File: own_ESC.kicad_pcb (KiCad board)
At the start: 2 copper layers, 61 x 99.6 mm, 144 parts, among them IC1 EFM8BB21F16G-C-QSOP24R, J1 SIGNAL PAD, J2 +BAT PAD, J3 -BAT PAD, J4 RX PAD, J5 CLK PAD, J6 A PAD, J7 B PAD, J8 C PAD, Q1 TPH1R403NL,L1Q, Q2 TPH1R403NL,L1Q, Q3 TPH1R403NL,L1Q, Q4 TPH1R403NL,L1Q, Q5 TPH1R403NL,L1Q, Q6 TPH1R403NL,L1Q, U1 FD6288T, U2 LM1117-5.0, U3 LM1117-3.3

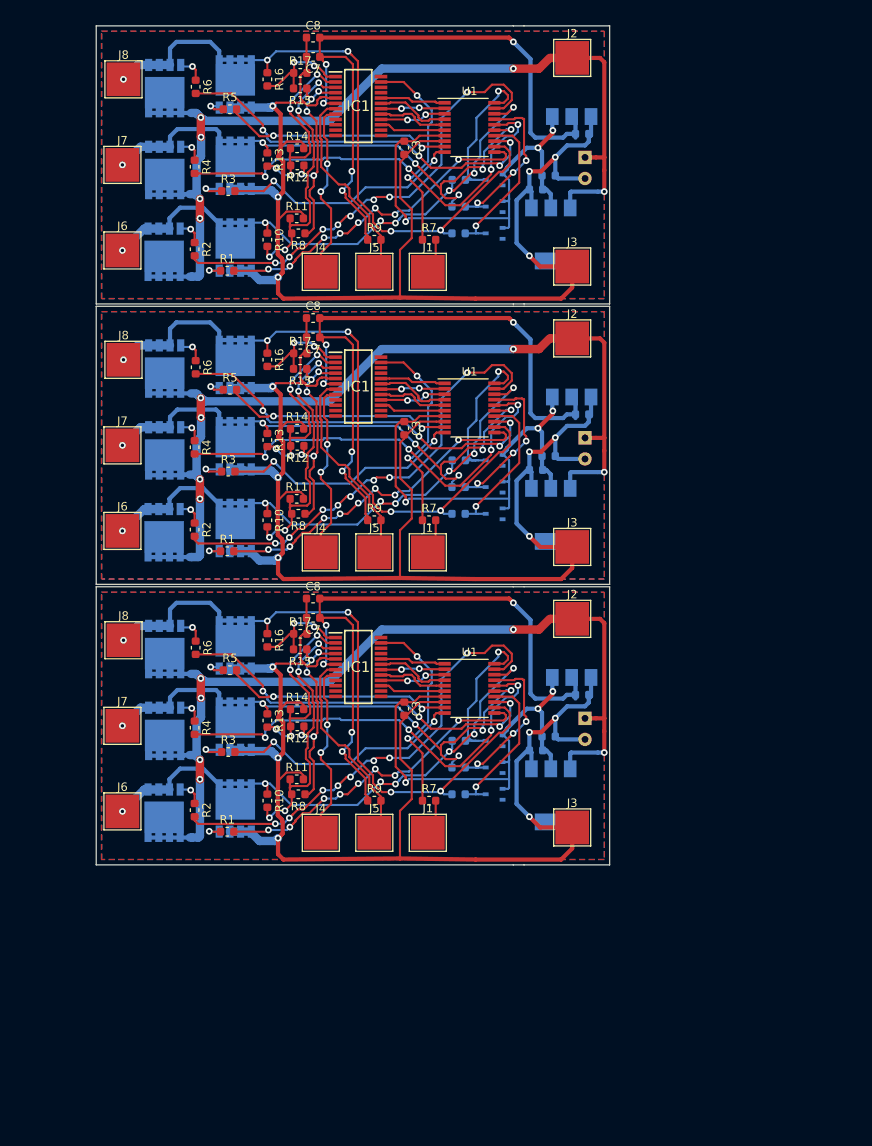
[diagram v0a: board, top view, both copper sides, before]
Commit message: Reduction of circuit area.
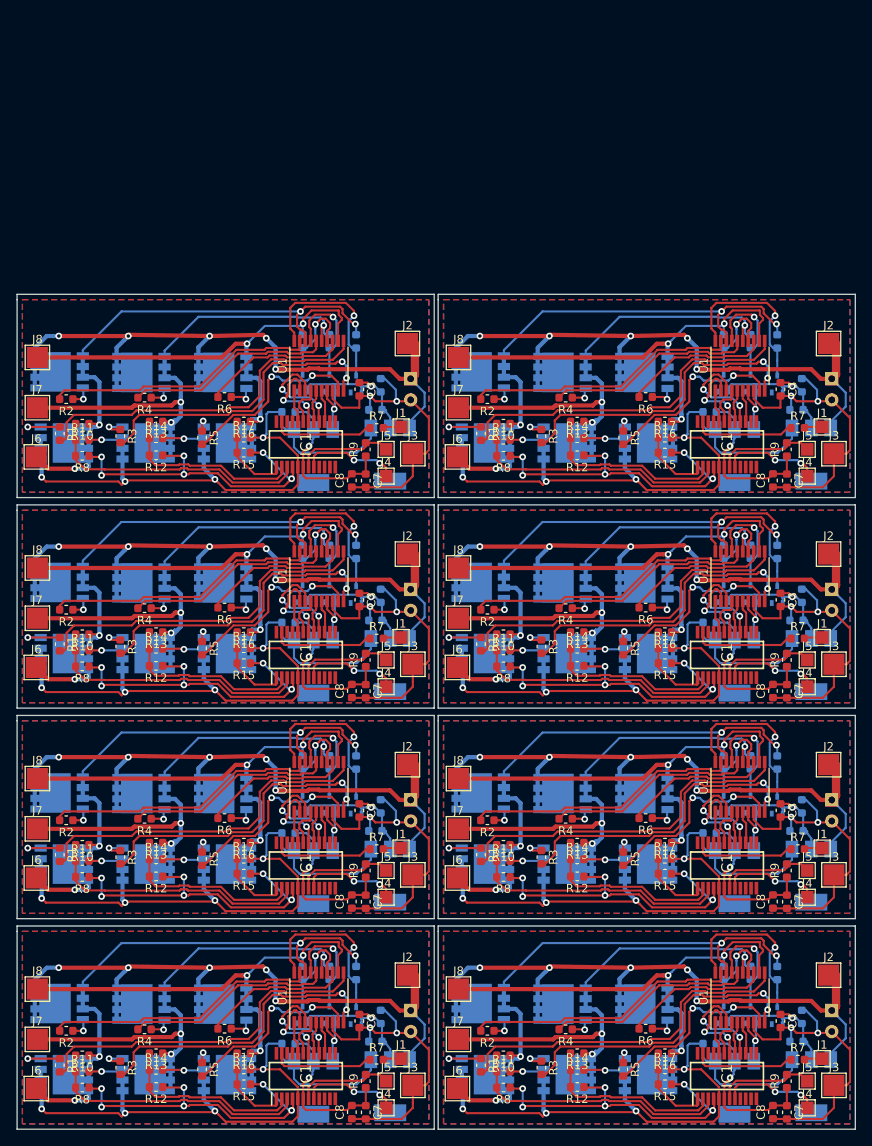
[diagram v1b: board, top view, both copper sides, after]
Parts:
- removed the C1 at (93.7, 118.4)
- removed the C1 at (93.7, 85.1)
- removed the C10 at (108.4, 113.0)
- removed the C10 at (108.4, 79.7)
- removed the C2 at (93.7, 121.6)
- removed the C2 at (93.7, 88.3)
- removed the C3 at (87.2, 114.6)
- removed the C3 at (87.2, 81.3)
- removed the C4 at (93.7, 124.8)
- removed the C4 at (93.7, 91.5)
- removed the C5 at (108.7, 115.7)
- removed the C5 at (108.7, 82.4)
- removed the C6 at (102.9, 119.6)
- removed the C6 at (102.9, 86.3)
- removed the C7 at (76.4, 103.8)
- removed the C7 at (76.4, 70.5)
- removed the C8 at (76.4, 101.5)
- removed the C8 at (76.4, 68.2)
- removed the C9 at (104.4, 117.9)
- removed the C9 at (104.4, 84.6)
- removed the D1 at (97.9, 118.4)
- removed the D1 at (97.9, 85.1)
- removed the D2 at (97.9, 121.6)
- removed the D2 at (97.9, 88.3)
- removed the D3 at (97.9, 124.8)
- removed the D3 at (97.9, 91.5)
- removed the IC1 at (81.8, 109.7)
- removed the IC1 at (81.8, 76.4)
- removed the J1 at (90.0, 129.3)
- removed the J1 at (90.0, 96.0)
- removed the J1 at (90.0, 62.7)
- removed the J2 at (107.2, 103.9)
- removed the J2 at (107.2, 70.6)
- removed the J2 at (107.2, 37.3)
- removed the J3 at (107.2, 128.7)
- removed the J3 at (107.2, 95.4)
- removed the J3 at (107.2, 62.1)
- removed the J4 at (77.3, 129.3)
- removed the J4 at (77.3, 96.0)
- removed the J4 at (77.3, 62.7)
- removed the J5 at (83.7, 129.3)
- removed the J5 at (83.7, 96.0)
- removed the J5 at (83.7, 62.7)
- removed the J6 at (53.8, 126.8)
- removed the J6 at (53.8, 93.5)
- removed the J6 at (53.8, 60.2)
- removed the J7 at (53.8, 116.6)
- removed the J7 at (53.8, 83.3)
- removed the J7 at (53.8, 50.0)
- removed the J8 at (53.9, 106.5)
- removed the J8 at (53.9, 73.2)
- removed the J8 at (53.9, 39.9)
- removed the Q1 at (67.2, 126.3)
- removed the Q1 at (67.2, 93.0)
- removed the Q2 at (58.7, 127.1)
- removed the Q2 at (58.7, 93.8)
- removed the Q3 at (67.2, 116.6)
- removed the Q3 at (67.2, 83.3)
- removed the Q4 at (58.8, 117.3)
- removed the Q4 at (58.8, 84.0)
- removed the Q5 at (67.2, 107.0)
- removed the Q5 at (67.2, 73.7)
- removed the Q6 at (58.8, 107.6)
- removed the Q6 at (58.8, 74.3)
- removed the R1 at (66.2, 129.2)
- removed the R1 at (66.2, 95.9)
- removed the R10 at (71.0, 125.5)
- removed the R10 at (71.0, 92.2)
- removed the R11 at (74.5, 123.0)
- removed the R11 at (74.5, 89.7)
- removed the R12 at (74.5, 116.7)
- removed the R12 at (74.5, 83.4)
- removed the R13 at (71.0, 116.0)
- removed the R13 at (71.0, 82.7)
- removed the R14 at (74.5, 114.7)
- removed the R14 at (74.5, 81.4)
- removed the R15 at (74.9, 107.6)
- removed the R15 at (74.9, 74.3)
- removed the R16 at (71.0, 106.5)
- removed the R16 at (71.0, 73.2)
- removed the R17 at (74.9, 105.7)
- removed the R17 at (74.9, 72.4)
- removed the R2 at (62.4, 126.6)
- removed the R2 at (62.4, 93.3)
- removed the R3 at (66.4, 119.7)
- removed the R3 at (66.4, 86.4)
- removed the R4 at (62.4, 116.9)
- removed the R4 at (62.4, 83.6)
- removed the R5 at (66.5, 110.0)
- removed the R5 at (66.5, 76.7)
- removed the R6 at (62.5, 107.4)
- removed the R6 at (62.5, 74.1)
- removed the R7 at (90.2, 125.5)
- removed the R7 at (90.2, 92.2)
- removed the R8 at (74.7, 124.8)
- removed the R8 at (74.7, 91.5)
- removed the R9 at (83.7, 125.5)
- removed the R9 at (83.7, 92.2)
- removed the U1 at (95.0, 112.2)
- removed the U1 at (95.0, 78.9)
- removed the U2 at (104.6, 124.9)
- removed the U2 at (104.6, 91.6)
- removed the U3 at (107.1, 107.7)
- removed the U3 at (107.1, 74.4)
- added C1: 1uF, Capacitor_SMD:C_0603_1608Metric, B.Cu at (131.5, 146.0)
- added C1: 1uF, Capacitor_SMD:C_0603_1608Metric, B.Cu at (81.5, 146.0)
- added C1: 1uF, Capacitor_SMD:C_0603_1608Metric, B.Cu at (131.5, 121.0)
- added C1: 1uF, Capacitor_SMD:C_0603_1608Metric, B.Cu at (81.5, 121.0)
- added C1: 1uF, Capacitor_SMD:C_0603_1608Metric, B.Cu at (131.5, 96.0)
- added C1: 1uF, Capacitor_SMD:C_0603_1608Metric, B.Cu at (81.5, 96.0)
- added C1: 1uF, Capacitor_SMD:C_0603_1608Metric, B.Cu at (131.5, 71.0)
- added C10: 10uF, Capacitor_SMD:C_0603_1608Metric, B.Cu at (123.5, 154.4)
- added C10: 10uF, Capacitor_SMD:C_0603_1608Metric, B.Cu at (73.5, 154.4)
- added C10: 10uF, Capacitor_SMD:C_0603_1608Metric, B.Cu at (123.5, 129.4)
- added C10: 10uF, Capacitor_SMD:C_0603_1608Metric, B.Cu at (73.5, 129.4)
- added C10: 10uF, Capacitor_SMD:C_0603_1608Metric, B.Cu at (123.5, 104.4)
- added C10: 10uF, Capacitor_SMD:C_0603_1608Metric, B.Cu at (73.5, 104.4)
- added C10: 10uF, Capacitor_SMD:C_0603_1608Metric, B.Cu at (123.5, 79.4)
- added C2: 1uF, Capacitor_SMD:C_0603_1608Metric, B.Cu at (128.4, 146.0)
- added C2: 1uF, Capacitor_SMD:C_0603_1608Metric, B.Cu at (78.4, 146.0)
- added C2: 1uF, Capacitor_SMD:C_0603_1608Metric, B.Cu at (128.4, 121.0)
- added C2: 1uF, Capacitor_SMD:C_0603_1608Metric, B.Cu at (78.4, 121.0)
- added C2: 1uF, Capacitor_SMD:C_0603_1608Metric, B.Cu at (128.4, 96.0)
- added C2: 1uF, Capacitor_SMD:C_0603_1608Metric, B.Cu at (78.4, 96.0)
- added C2: 1uF, Capacitor_SMD:C_0603_1608Metric, B.Cu at (128.4, 71.0)
- added C3: 10uF, Capacitor_SMD:C_0603_1608Metric, F.Cu at (131.9, 151.7)
- added C3: 10uF, Capacitor_SMD:C_0603_1608Metric, F.Cu at (81.9, 151.7)
- added C3: 10uF, Capacitor_SMD:C_0603_1608Metric, F.Cu at (131.9, 126.7)
- added C3: 10uF, Capacitor_SMD:C_0603_1608Metric, F.Cu at (81.9, 126.7)
- added C3: 10uF, Capacitor_SMD:C_0603_1608Metric, F.Cu at (131.9, 101.7)
- added C3: 10uF, Capacitor_SMD:C_0603_1608Metric, F.Cu at (81.9, 101.7)
- added C3: 10uF, Capacitor_SMD:C_0603_1608Metric, F.Cu at (131.9, 76.7)
- added C4: 1uF, Capacitor_SMD:C_0603_1608Metric, B.Cu at (125.2, 146.0)
- added C4: 1uF, Capacitor_SMD:C_0603_1608Metric, B.Cu at (75.2, 146.0)
- added C4: 1uF, Capacitor_SMD:C_0603_1608Metric, B.Cu at (125.2, 121.0)
- added C4: 1uF, Capacitor_SMD:C_0603_1608Metric, B.Cu at (75.2, 121.0)
- added C4: 1uF, Capacitor_SMD:C_0603_1608Metric, B.Cu at (125.2, 96.0)
- added C4: 1uF, Capacitor_SMD:C_0603_1608Metric, B.Cu at (75.2, 96.0)
- added C4: 1uF, Capacitor_SMD:C_0603_1608Metric, B.Cu at (125.2, 71.0)
- added C5: 10uF, Capacitor_THT:CP_Radial_D5.0mm_P2.50mm, B.Cu at (138.0, 150.4)
- added C5: 10uF, Capacitor_THT:CP_Radial_D5.0mm_P2.50mm, B.Cu at (88.0, 150.4)
- added C5: 10uF, Capacitor_THT:CP_Radial_D5.0mm_P2.50mm, B.Cu at (138.0, 125.4)
- added C5: 10uF, Capacitor_THT:CP_Radial_D5.0mm_P2.50mm, B.Cu at (88.0, 125.4)
- added C5: 10uF, Capacitor_THT:CP_Radial_D5.0mm_P2.50mm, B.Cu at (138.0, 100.4)
- added C5: 10uF, Capacitor_THT:CP_Radial_D5.0mm_P2.50mm, B.Cu at (88.0, 100.4)
- added C5: 10uF, Capacitor_THT:CP_Radial_D5.0mm_P2.50mm, B.Cu at (138.0, 75.4)
- added C6: 10uF, Capacitor_SMD:C_0603_1608Metric, B.Cu at (133.8, 154.1)
- added C6: 10uF, Capacitor_SMD:C_0603_1608Metric, B.Cu at (83.8, 154.1)
- added C6: 10uF, Capacitor_SMD:C_0603_1608Metric, B.Cu at (133.8, 129.1)
- added C6: 10uF, Capacitor_SMD:C_0603_1608Metric, B.Cu at (83.8, 129.1)
- added C6: 10uF, Capacitor_SMD:C_0603_1608Metric, B.Cu at (133.8, 104.1)
- added C6: 10uF, Capacitor_SMD:C_0603_1608Metric, B.Cu at (83.8, 104.1)
- added C6: 10uF, Capacitor_SMD:C_0603_1608Metric, B.Cu at (133.8, 79.1)
- added C7: 0.1uF, Capacitor_SMD:C_0603_1608Metric, F.Cu at (132.7, 162.5)
- added C7: 0.1uF, Capacitor_SMD:C_0603_1608Metric, F.Cu at (82.7, 162.5)
- added C7: 0.1uF, Capacitor_SMD:C_0603_1608Metric, F.Cu at (132.7, 137.5)
- added C7: 0.1uF, Capacitor_SMD:C_0603_1608Metric, F.Cu at (82.7, 137.5)
- added C7: 0.1uF, Capacitor_SMD:C_0603_1608Metric, F.Cu at (132.7, 112.5)
- added C7: 0.1uF, Capacitor_SMD:C_0603_1608Metric, F.Cu at (82.7, 112.5)
- added C7: 0.1uF, Capacitor_SMD:C_0603_1608Metric, F.Cu at (132.7, 87.5)
- added C8: 4.7uF, Capacitor_SMD:C_0603_1608Metric, F.Cu at (131.0, 162.5)
- added C8: 4.7uF, Capacitor_SMD:C_0603_1608Metric, F.Cu at (81.0, 162.5)
- added C8: 4.7uF, Capacitor_SMD:C_0603_1608Metric, F.Cu at (131.0, 137.5)
- added C8: 4.7uF, Capacitor_SMD:C_0603_1608Metric, F.Cu at (81.0, 137.5)
- added C8: 4.7uF, Capacitor_SMD:C_0603_1608Metric, F.Cu at (131.0, 112.5)
- added C8: 4.7uF, Capacitor_SMD:C_0603_1608Metric, F.Cu at (81.0, 112.5)
- added C8: 4.7uF, Capacitor_SMD:C_0603_1608Metric, F.Cu at (131.0, 87.5)
- added C9: 10uF, Capacitor_SMD:C_0603_1608Metric, B.Cu at (134.5, 151.2)
- added C9: 10uF, Capacitor_SMD:C_0603_1608Metric, B.Cu at (84.5, 151.2)
- added C9: 10uF, Capacitor_SMD:C_0603_1608Metric, B.Cu at (134.5, 126.2)
- added C9: 10uF, Capacitor_SMD:C_0603_1608Metric, B.Cu at (84.5, 126.2)
- added C9: 10uF, Capacitor_SMD:C_0603_1608Metric, B.Cu at (134.5, 101.2)
- added C9: 10uF, Capacitor_SMD:C_0603_1608Metric, B.Cu at (84.5, 101.2)
- added C9: 10uF, Capacitor_SMD:C_0603_1608Metric, B.Cu at (134.5, 76.2)
- added D1: BAT54W, Package_TO_SOT_SMD:SOT-323_SC-70, B.Cu at (131.5, 151.1)
- added D1: BAT54W, Package_TO_SOT_SMD:SOT-323_SC-70, B.Cu at (81.5, 151.1)
- added D1: BAT54W, Package_TO_SOT_SMD:SOT-323_SC-70, B.Cu at (131.5, 126.1)
- added D1: BAT54W, Package_TO_SOT_SMD:SOT-323_SC-70, B.Cu at (81.5, 126.1)
- added D1: BAT54W, Package_TO_SOT_SMD:SOT-323_SC-70, B.Cu at (131.5, 101.1)
- added D1: BAT54W, Package_TO_SOT_SMD:SOT-323_SC-70, B.Cu at (81.5, 101.1)
- added D1: BAT54W, Package_TO_SOT_SMD:SOT-323_SC-70, B.Cu at (131.5, 76.1)
- added D2: BAT54W, Package_TO_SOT_SMD:SOT-323_SC-70, B.Cu at (128.4, 151.0)
- added D2: BAT54W, Package_TO_SOT_SMD:SOT-323_SC-70, B.Cu at (78.4, 151.0)
- added D2: BAT54W, Package_TO_SOT_SMD:SOT-323_SC-70, B.Cu at (128.4, 126.0)
- added D2: BAT54W, Package_TO_SOT_SMD:SOT-323_SC-70, B.Cu at (78.4, 126.0)
- added D2: BAT54W, Package_TO_SOT_SMD:SOT-323_SC-70, B.Cu at (128.4, 101.0)
- added D2: BAT54W, Package_TO_SOT_SMD:SOT-323_SC-70, B.Cu at (78.4, 101.0)
- added D2: BAT54W, Package_TO_SOT_SMD:SOT-323_SC-70, B.Cu at (128.4, 76.0)
- added D3: BAT54W, Package_TO_SOT_SMD:SOT-323_SC-70, B.Cu at (125.2, 151.0)
- added D3: BAT54W, Package_TO_SOT_SMD:SOT-323_SC-70, B.Cu at (75.2, 151.0)
- added D3: BAT54W, Package_TO_SOT_SMD:SOT-323_SC-70, B.Cu at (125.2, 126.0)
- added D3: BAT54W, Package_TO_SOT_SMD:SOT-323_SC-70, B.Cu at (75.2, 126.0)
- added D3: BAT54W, Package_TO_SOT_SMD:SOT-323_SC-70, B.Cu at (125.2, 101.0)
- added D3: BAT54W, Package_TO_SOT_SMD:SOT-323_SC-70, B.Cu at (75.2, 101.0)
- added D3: BAT54W, Package_TO_SOT_SMD:SOT-323_SC-70, B.Cu at (125.2, 76.0)
- added IC1: EFM8BB21F16G-C-QSOP24R, SOP64P600X175-24N, F.Cu at (125.6, 158.2)
- added IC1: EFM8BB21F16G-C-QSOP24R, SOP64P600X175-24N, F.Cu at (75.6, 158.2)
- added IC1: EFM8BB21F16G-C-QSOP24R, SOP64P600X175-24N, F.Cu at (125.6, 133.2)
- added IC1: EFM8BB21F16G-C-QSOP24R, SOP64P600X175-24N, F.Cu at (75.6, 133.2)
- added IC1: EFM8BB21F16G-C-QSOP24R, SOP64P600X175-24N, F.Cu at (125.6, 108.2)
- added IC1: EFM8BB21F16G-C-QSOP24R, SOP64P600X175-24N, F.Cu at (75.6, 108.2)
- added IC1: EFM8BB21F16G-C-QSOP24R, SOP64P600X175-24N, F.Cu at (125.6, 83.2)
- added J1: SIGNAL PAD, TestPoint:TestPoint_Pad_1.5x1.5mm, F.Cu at (136.9, 156.2)
- added J1: SIGNAL PAD, TestPoint:TestPoint_Pad_1.5x1.5mm, F.Cu at (86.9, 156.2)
- added J1: SIGNAL PAD, TestPoint:TestPoint_Pad_1.5x1.5mm, F.Cu at (136.9, 131.2)
- added J1: SIGNAL PAD, TestPoint:TestPoint_Pad_1.5x1.5mm, F.Cu at (86.9, 131.2)
- added J1: SIGNAL PAD, TestPoint:TestPoint_Pad_1.5x1.5mm, F.Cu at (136.9, 106.2)
- added J1: SIGNAL PAD, TestPoint:TestPoint_Pad_1.5x1.5mm, F.Cu at (86.9, 106.2)
- added J1: SIGNAL PAD, TestPoint:TestPoint_Pad_1.5x1.5mm, F.Cu at (136.9, 81.2)
- added J1: SIGNAL PAD, TestPoint:TestPoint_Pad_1.5x1.5mm, F.Cu at (86.9, 81.2)
- added J2: +BAT PAD, TestPoint:TestPoint_Pad_2.5x2.5mm, F.Cu at (137.6, 146.2)
- added J2: +BAT PAD, TestPoint:TestPoint_Pad_2.5x2.5mm, F.Cu at (87.6, 146.2)
- added J2: +BAT PAD, TestPoint:TestPoint_Pad_2.5x2.5mm, F.Cu at (137.6, 121.2)
- added J2: +BAT PAD, TestPoint:TestPoint_Pad_2.5x2.5mm, F.Cu at (87.6, 121.2)
- added J2: +BAT PAD, TestPoint:TestPoint_Pad_2.5x2.5mm, F.Cu at (137.6, 96.2)
- added J2: +BAT PAD, TestPoint:TestPoint_Pad_2.5x2.5mm, F.Cu at (87.6, 96.2)
- added J2: +BAT PAD, TestPoint:TestPoint_Pad_2.5x2.5mm, F.Cu at (137.6, 71.2)
- added J2: +BAT PAD, TestPoint:TestPoint_Pad_2.5x2.5mm, F.Cu at (87.6, 71.2)
- added J3: -BAT PAD, TestPoint:TestPoint_Pad_2.5x2.5mm, F.Cu at (138.3, 159.3)
- added J3: -BAT PAD, TestPoint:TestPoint_Pad_2.5x2.5mm, F.Cu at (88.3, 159.3)
- added J3: -BAT PAD, TestPoint:TestPoint_Pad_2.5x2.5mm, F.Cu at (138.3, 134.3)
- added J3: -BAT PAD, TestPoint:TestPoint_Pad_2.5x2.5mm, F.Cu at (88.3, 134.3)
- added J3: -BAT PAD, TestPoint:TestPoint_Pad_2.5x2.5mm, F.Cu at (138.3, 109.3)
- added J3: -BAT PAD, TestPoint:TestPoint_Pad_2.5x2.5mm, F.Cu at (88.3, 109.3)
- added J3: -BAT PAD, TestPoint:TestPoint_Pad_2.5x2.5mm, F.Cu at (138.3, 84.3)
- added J3: -BAT PAD, TestPoint:TestPoint_Pad_2.5x2.5mm, F.Cu at (88.3, 84.3)
- added J4: RX PAD, TestPoint:TestPoint_Pad_1.5x1.5mm, F.Cu at (135.1, 162.0)
- added J4: RX PAD, TestPoint:TestPoint_Pad_1.5x1.5mm, F.Cu at (85.1, 162.0)
- added J4: RX PAD, TestPoint:TestPoint_Pad_1.5x1.5mm, F.Cu at (135.1, 137.0)
- added J4: RX PAD, TestPoint:TestPoint_Pad_1.5x1.5mm, F.Cu at (85.1, 137.0)
- added J4: RX PAD, TestPoint:TestPoint_Pad_1.5x1.5mm, F.Cu at (135.1, 112.0)
- added J4: RX PAD, TestPoint:TestPoint_Pad_1.5x1.5mm, F.Cu at (85.1, 112.0)
- added J4: RX PAD, TestPoint:TestPoint_Pad_1.5x1.5mm, F.Cu at (135.1, 87.0)
- added J4: RX PAD, TestPoint:TestPoint_Pad_1.5x1.5mm, F.Cu at (85.1, 87.0)
- added J5: CLK PAD, TestPoint:TestPoint_Pad_1.5x1.5mm, F.Cu at (135.1, 158.8)
- added J5: CLK PAD, TestPoint:TestPoint_Pad_1.5x1.5mm, F.Cu at (85.1, 158.8)
- added J5: CLK PAD, TestPoint:TestPoint_Pad_1.5x1.5mm, F.Cu at (135.1, 133.8)
- added J5: CLK PAD, TestPoint:TestPoint_Pad_1.5x1.5mm, F.Cu at (85.1, 133.8)
- added J5: CLK PAD, TestPoint:TestPoint_Pad_1.5x1.5mm, F.Cu at (135.1, 108.8)
- added J5: CLK PAD, TestPoint:TestPoint_Pad_1.5x1.5mm, F.Cu at (85.1, 108.8)
- added J5: CLK PAD, TestPoint:TestPoint_Pad_1.5x1.5mm, F.Cu at (135.1, 83.8)
- added J5: CLK PAD, TestPoint:TestPoint_Pad_1.5x1.5mm, F.Cu at (85.1, 83.8)
- added J6: A PAD, TestPoint:TestPoint_Pad_2.5x2.5mm, F.Cu at (93.6, 159.7)
- added J6: A PAD, TestPoint:TestPoint_Pad_2.5x2.5mm, F.Cu at (43.6, 159.7)
- added J6: A PAD, TestPoint:TestPoint_Pad_2.5x2.5mm, F.Cu at (93.6, 134.7)
- added J6: A PAD, TestPoint:TestPoint_Pad_2.5x2.5mm, F.Cu at (43.6, 134.7)
- added J6: A PAD, TestPoint:TestPoint_Pad_2.5x2.5mm, F.Cu at (93.6, 109.7)
- added J6: A PAD, TestPoint:TestPoint_Pad_2.5x2.5mm, F.Cu at (43.6, 109.7)
- added J6: A PAD, TestPoint:TestPoint_Pad_2.5x2.5mm, F.Cu at (93.6, 84.7)
- added J6: A PAD, TestPoint:TestPoint_Pad_2.5x2.5mm, F.Cu at (43.6, 84.7)
- added J7: B PAD, TestPoint:TestPoint_Pad_2.5x2.5mm, F.Cu at (93.7, 153.9)
- added J7: B PAD, TestPoint:TestPoint_Pad_2.5x2.5mm, F.Cu at (43.7, 153.9)
- added J7: B PAD, TestPoint:TestPoint_Pad_2.5x2.5mm, F.Cu at (93.7, 128.9)
- added J7: B PAD, TestPoint:TestPoint_Pad_2.5x2.5mm, F.Cu at (43.7, 128.9)
- added J7: B PAD, TestPoint:TestPoint_Pad_2.5x2.5mm, F.Cu at (93.7, 103.9)
- added J7: B PAD, TestPoint:TestPoint_Pad_2.5x2.5mm, F.Cu at (43.7, 103.9)
- added J7: B PAD, TestPoint:TestPoint_Pad_2.5x2.5mm, F.Cu at (93.7, 78.9)
- added J7: B PAD, TestPoint:TestPoint_Pad_2.5x2.5mm, F.Cu at (43.7, 78.9)
- added J8: C PAD, TestPoint:TestPoint_Pad_2.5x2.5mm, F.Cu at (93.7, 147.9)
- added J8: C PAD, TestPoint:TestPoint_Pad_2.5x2.5mm, F.Cu at (43.7, 147.9)
- added J8: C PAD, TestPoint:TestPoint_Pad_2.5x2.5mm, F.Cu at (93.7, 122.9)
- added J8: C PAD, TestPoint:TestPoint_Pad_2.5x2.5mm, F.Cu at (43.7, 122.9)
- added J8: C PAD, TestPoint:TestPoint_Pad_2.5x2.5mm, F.Cu at (93.7, 97.9)
- added J8: C PAD, TestPoint:TestPoint_Pad_2.5x2.5mm, F.Cu at (43.7, 97.9)
- added J8: C PAD, TestPoint:TestPoint_Pad_2.5x2.5mm, F.Cu at (93.7, 72.9)
- added J8: C PAD, TestPoint:TestPoint_Pad_2.5x2.5mm, F.Cu at (43.7, 72.9)
- added Q1: TPH1R403NL,L1Q, TPH1R403NLL1Q, B.Cu at (96.9, 158.1)
- added Q1: TPH1R403NL,L1Q, TPH1R403NLL1Q, B.Cu at (46.9, 158.1)
- added Q1: TPH1R403NL,L1Q, TPH1R403NLL1Q, B.Cu at (96.9, 133.1)
- added Q1: TPH1R403NL,L1Q, TPH1R403NLL1Q, B.Cu at (46.9, 133.1)
- added Q1: TPH1R403NL,L1Q, TPH1R403NLL1Q, B.Cu at (96.9, 108.1)
- added Q1: TPH1R403NL,L1Q, TPH1R403NLL1Q, B.Cu at (46.9, 108.1)
- added Q1: TPH1R403NL,L1Q, TPH1R403NLL1Q, B.Cu at (96.9, 83.1)
- added Q2: TPH1R403NL,L1Q, TPH1R403NLL1Q, B.Cu at (96.2, 149.6)
- added Q2: TPH1R403NL,L1Q, TPH1R403NLL1Q, B.Cu at (46.2, 149.6)
- added Q2: TPH1R403NL,L1Q, TPH1R403NLL1Q, B.Cu at (96.2, 124.6)
- added Q2: TPH1R403NL,L1Q, TPH1R403NLL1Q, B.Cu at (46.2, 124.6)
- added Q2: TPH1R403NL,L1Q, TPH1R403NLL1Q, B.Cu at (96.2, 99.6)
- added Q2: TPH1R403NL,L1Q, TPH1R403NLL1Q, B.Cu at (46.2, 99.6)
- added Q2: TPH1R403NL,L1Q, TPH1R403NLL1Q, B.Cu at (96.2, 74.6)
- added Q3: TPH1R403NL,L1Q, TPH1R403NLL1Q, B.Cu at (106.6, 158.1)
- added Q3: TPH1R403NL,L1Q, TPH1R403NLL1Q, B.Cu at (56.6, 158.1)
- added Q3: TPH1R403NL,L1Q, TPH1R403NLL1Q, B.Cu at (106.6, 133.1)
- added Q3: TPH1R403NL,L1Q, TPH1R403NLL1Q, B.Cu at (56.6, 133.1)
- added Q3: TPH1R403NL,L1Q, TPH1R403NLL1Q, B.Cu at (106.6, 108.1)
- added Q3: TPH1R403NL,L1Q, TPH1R403NLL1Q, B.Cu at (56.6, 108.1)
- added Q3: TPH1R403NL,L1Q, TPH1R403NLL1Q, B.Cu at (106.6, 83.1)
- added Q4: TPH1R403NL,L1Q, TPH1R403NLL1Q, B.Cu at (105.9, 149.7)
- added Q4: TPH1R403NL,L1Q, TPH1R403NLL1Q, B.Cu at (55.9, 149.7)
- added Q4: TPH1R403NL,L1Q, TPH1R403NLL1Q, B.Cu at (105.9, 124.7)
- added Q4: TPH1R403NL,L1Q, TPH1R403NLL1Q, B.Cu at (55.9, 124.7)
- added Q4: TPH1R403NL,L1Q, TPH1R403NLL1Q, B.Cu at (105.9, 99.7)
- added Q4: TPH1R403NL,L1Q, TPH1R403NLL1Q, B.Cu at (55.9, 99.7)
- added Q4: TPH1R403NL,L1Q, TPH1R403NLL1Q, B.Cu at (105.9, 74.7)
- added Q5: TPH1R403NL,L1Q, TPH1R403NLL1Q, B.Cu at (116.3, 158.1)
- added Q5: TPH1R403NL,L1Q, TPH1R403NLL1Q, B.Cu at (66.3, 158.1)
- added Q5: TPH1R403NL,L1Q, TPH1R403NLL1Q, B.Cu at (116.3, 133.1)
- added Q5: TPH1R403NL,L1Q, TPH1R403NLL1Q, B.Cu at (66.3, 133.1)
- added Q5: TPH1R403NL,L1Q, TPH1R403NLL1Q, B.Cu at (116.3, 108.1)
- added Q5: TPH1R403NL,L1Q, TPH1R403NLL1Q, B.Cu at (66.3, 108.1)
- added Q5: TPH1R403NL,L1Q, TPH1R403NLL1Q, B.Cu at (116.3, 83.1)
- added Q6: TPH1R403NL,L1Q, TPH1R403NLL1Q, B.Cu at (115.7, 149.7)
- added Q6: TPH1R403NL,L1Q, TPH1R403NLL1Q, B.Cu at (65.7, 149.7)
- added Q6: TPH1R403NL,L1Q, TPH1R403NLL1Q, B.Cu at (115.7, 124.7)
- added Q6: TPH1R403NL,L1Q, TPH1R403NLL1Q, B.Cu at (65.7, 124.7)
- added Q6: TPH1R403NL,L1Q, TPH1R403NLL1Q, B.Cu at (115.7, 99.7)
- added Q6: TPH1R403NL,L1Q, TPH1R403NLL1Q, B.Cu at (65.7, 99.7)
- added Q6: TPH1R403NL,L1Q, TPH1R403NLL1Q, B.Cu at (115.7, 74.7)
- added R1: 25, Capacitor_SMD:C_0603_1608Metric, F.Cu at (96.4, 156.9)
- added R1: 25, Capacitor_SMD:C_0603_1608Metric, F.Cu at (46.4, 156.9)
- added R1: 25, Capacitor_SMD:C_0603_1608Metric, F.Cu at (96.4, 131.9)
- added R1: 25, Capacitor_SMD:C_0603_1608Metric, F.Cu at (46.4, 131.9)
- added R1: 25, Capacitor_SMD:C_0603_1608Metric, F.Cu at (96.4, 106.9)
- added R1: 25, Capacitor_SMD:C_0603_1608Metric, F.Cu at (46.4, 106.9)
- added R1: 25, Capacitor_SMD:C_0603_1608Metric, F.Cu at (96.4, 81.9)
- added R10: 10k, Capacitor_SMD:C_0603_1608Metric, F.Cu at (99.0, 155.8)
- added R10: 10k, Capacitor_SMD:C_0603_1608Metric, F.Cu at (49.0, 155.8)
- added R10: 10k, Capacitor_SMD:C_0603_1608Metric, F.Cu at (99.0, 130.8)
- added R10: 10k, Capacitor_SMD:C_0603_1608Metric, F.Cu at (49.0, 130.8)
- added R10: 10k, Capacitor_SMD:C_0603_1608Metric, F.Cu at (99.0, 105.8)
- added R10: 10k, Capacitor_SMD:C_0603_1608Metric, F.Cu at (49.0, 105.8)
- added R10: 10k, Capacitor_SMD:C_0603_1608Metric, F.Cu at (99.0, 80.8)
- added R11: 1k, Capacitor_SMD:C_0603_1608Metric, F.Cu at (99.0, 157.7)
- added R11: 1k, Capacitor_SMD:C_0603_1608Metric, F.Cu at (49.0, 157.7)
- added R11: 1k, Capacitor_SMD:C_0603_1608Metric, F.Cu at (99.0, 132.7)
- added R11: 1k, Capacitor_SMD:C_0603_1608Metric, F.Cu at (49.0, 132.7)
- added R11: 1k, Capacitor_SMD:C_0603_1608Metric, F.Cu at (99.0, 107.7)
- added R11: 1k, Capacitor_SMD:C_0603_1608Metric, F.Cu at (49.0, 107.7)
- added R11: 1k, Capacitor_SMD:C_0603_1608Metric, F.Cu at (99.0, 82.7)
- added R12: 4k, Capacitor_SMD:C_0603_1608Metric, F.Cu at (107.8, 159.5)
- added R12: 4k, Capacitor_SMD:C_0603_1608Metric, F.Cu at (57.8, 159.5)
- added R12: 4k, Capacitor_SMD:C_0603_1608Metric, F.Cu at (107.8, 134.5)
- added R12: 4k, Capacitor_SMD:C_0603_1608Metric, F.Cu at (57.8, 134.5)
- added R12: 4k, Capacitor_SMD:C_0603_1608Metric, F.Cu at (107.8, 109.5)
- added R12: 4k, Capacitor_SMD:C_0603_1608Metric, F.Cu at (57.8, 109.5)
- added R12: 4k, Capacitor_SMD:C_0603_1608Metric, F.Cu at (107.8, 84.5)
- added R13: 10k, Capacitor_SMD:C_0603_1608Metric, F.Cu at (107.8, 155.5)
- added R13: 10k, Capacitor_SMD:C_0603_1608Metric, F.Cu at (57.8, 155.5)
- added R13: 10k, Capacitor_SMD:C_0603_1608Metric, F.Cu at (107.8, 130.5)
- added R13: 10k, Capacitor_SMD:C_0603_1608Metric, F.Cu at (57.8, 130.5)
- added R13: 10k, Capacitor_SMD:C_0603_1608Metric, F.Cu at (107.8, 105.5)
- added R13: 10k, Capacitor_SMD:C_0603_1608Metric, F.Cu at (57.8, 105.5)
- added R13: 10k, Capacitor_SMD:C_0603_1608Metric, F.Cu at (107.8, 80.5)
- added R14: 1k, Capacitor_SMD:C_0603_1608Metric, F.Cu at (107.8, 157.5)
- added R14: 1k, Capacitor_SMD:C_0603_1608Metric, F.Cu at (57.8, 157.5)
- added R14: 1k, Capacitor_SMD:C_0603_1608Metric, F.Cu at (107.8, 132.5)
- added R14: 1k, Capacitor_SMD:C_0603_1608Metric, F.Cu at (57.8, 132.5)
- added R14: 1k, Capacitor_SMD:C_0603_1608Metric, F.Cu at (107.8, 107.5)
- added R14: 1k, Capacitor_SMD:C_0603_1608Metric, F.Cu at (57.8, 107.5)
- added R14: 1k, Capacitor_SMD:C_0603_1608Metric, F.Cu at (107.8, 82.5)
- added R15: 4k, Capacitor_SMD:C_0603_1608Metric, F.Cu at (118.2, 159.2)
- added R15: 4k, Capacitor_SMD:C_0603_1608Metric, F.Cu at (68.2, 159.2)
- added R15: 4k, Capacitor_SMD:C_0603_1608Metric, F.Cu at (118.2, 134.2)
- added R15: 4k, Capacitor_SMD:C_0603_1608Metric, F.Cu at (68.2, 134.2)
- added R15: 4k, Capacitor_SMD:C_0603_1608Metric, F.Cu at (118.2, 109.2)
- added R15: 4k, Capacitor_SMD:C_0603_1608Metric, F.Cu at (68.2, 109.2)
- added R15: 4k, Capacitor_SMD:C_0603_1608Metric, F.Cu at (118.2, 84.2)
- added R16: 10k, Capacitor_SMD:C_0603_1608Metric, F.Cu at (118.2, 155.5)
- added R16: 10k, Capacitor_SMD:C_0603_1608Metric, F.Cu at (68.2, 155.5)
- added R16: 10k, Capacitor_SMD:C_0603_1608Metric, F.Cu at (118.2, 130.5)
- added R16: 10k, Capacitor_SMD:C_0603_1608Metric, F.Cu at (68.2, 130.5)
- added R16: 10k, Capacitor_SMD:C_0603_1608Metric, F.Cu at (118.2, 105.5)
- added R16: 10k, Capacitor_SMD:C_0603_1608Metric, F.Cu at (68.2, 105.5)
- added R16: 10k, Capacitor_SMD:C_0603_1608Metric, F.Cu at (118.2, 80.5)
- added R17: 1k, Capacitor_SMD:C_0603_1608Metric, F.Cu at (118.2, 157.4)
- added R17: 1k, Capacitor_SMD:C_0603_1608Metric, F.Cu at (68.2, 157.4)
- added R17: 1k, Capacitor_SMD:C_0603_1608Metric, F.Cu at (118.2, 132.4)
- added R17: 1k, Capacitor_SMD:C_0603_1608Metric, F.Cu at (68.2, 132.4)
- added R17: 1k, Capacitor_SMD:C_0603_1608Metric, F.Cu at (118.2, 107.4)
- added R17: 1k, Capacitor_SMD:C_0603_1608Metric, F.Cu at (68.2, 107.4)
- added R17: 1k, Capacitor_SMD:C_0603_1608Metric, F.Cu at (118.2, 82.4)
- added R2: 25, Capacitor_SMD:C_0603_1608Metric, F.Cu at (97.1, 152.9)
- added R2: 25, Capacitor_SMD:C_0603_1608Metric, F.Cu at (47.1, 152.9)
- added R2: 25, Capacitor_SMD:C_0603_1608Metric, F.Cu at (97.1, 127.9)
- added R2: 25, Capacitor_SMD:C_0603_1608Metric, F.Cu at (47.1, 127.9)
- added R2: 25, Capacitor_SMD:C_0603_1608Metric, F.Cu at (97.1, 102.9)
- added R2: 25, Capacitor_SMD:C_0603_1608Metric, F.Cu at (47.1, 102.9)
- added R2: 25, Capacitor_SMD:C_0603_1608Metric, F.Cu at (97.1, 77.9)
- added R3: 25, Capacitor_SMD:C_0603_1608Metric, F.Cu at (103.5, 157.2)
- added R3: 25, Capacitor_SMD:C_0603_1608Metric, F.Cu at (53.5, 157.2)
- added R3: 25, Capacitor_SMD:C_0603_1608Metric, F.Cu at (103.5, 132.2)
- added R3: 25, Capacitor_SMD:C_0603_1608Metric, F.Cu at (53.5, 132.2)
- added R3: 25, Capacitor_SMD:C_0603_1608Metric, F.Cu at (103.5, 107.2)
- added R3: 25, Capacitor_SMD:C_0603_1608Metric, F.Cu at (53.5, 107.2)
- added R3: 25, Capacitor_SMD:C_0603_1608Metric, F.Cu at (103.5, 82.2)
- added R4: 25, Capacitor_SMD:C_0603_1608Metric, F.Cu at (106.4, 152.7)
- added R4: 25, Capacitor_SMD:C_0603_1608Metric, F.Cu at (56.4, 152.7)
- added R4: 25, Capacitor_SMD:C_0603_1608Metric, F.Cu at (106.4, 127.7)
- added R4: 25, Capacitor_SMD:C_0603_1608Metric, F.Cu at (56.4, 127.7)
- added R4: 25, Capacitor_SMD:C_0603_1608Metric, F.Cu at (106.4, 102.7)
- added R4: 25, Capacitor_SMD:C_0603_1608Metric, F.Cu at (56.4, 102.7)
- added R4: 25, Capacitor_SMD:C_0603_1608Metric, F.Cu at (106.4, 77.7)
- added R5: 25, Capacitor_SMD:C_0603_1608Metric, F.Cu at (113.2, 157.4)
- added R5: 25, Capacitor_SMD:C_0603_1608Metric, F.Cu at (63.2, 157.4)
- added R5: 25, Capacitor_SMD:C_0603_1608Metric, F.Cu at (113.2, 132.4)
- added R5: 25, Capacitor_SMD:C_0603_1608Metric, F.Cu at (63.2, 132.4)
- added R5: 25, Capacitor_SMD:C_0603_1608Metric, F.Cu at (113.2, 107.4)
- added R5: 25, Capacitor_SMD:C_0603_1608Metric, F.Cu at (63.2, 107.4)
- added R5: 25, Capacitor_SMD:C_0603_1608Metric, F.Cu at (113.2, 82.4)
- added R6: 25, Capacitor_SMD:C_0603_1608Metric, F.Cu at (115.9, 152.6)
- added R6: 25, Capacitor_SMD:C_0603_1608Metric, F.Cu at (65.9, 152.6)
- added R6: 25, Capacitor_SMD:C_0603_1608Metric, F.Cu at (115.9, 127.6)
- added R6: 25, Capacitor_SMD:C_0603_1608Metric, F.Cu at (65.9, 127.6)
- added R6: 25, Capacitor_SMD:C_0603_1608Metric, F.Cu at (115.9, 102.6)
- added R6: 25, Capacitor_SMD:C_0603_1608Metric, F.Cu at (65.9, 102.6)
- added R6: 25, Capacitor_SMD:C_0603_1608Metric, F.Cu at (115.9, 77.6)
- added R7: 1k, Capacitor_SMD:C_0603_1608Metric, F.Cu at (134.0, 156.3)
- added R7: 1k, Capacitor_SMD:C_0603_1608Metric, F.Cu at (84.0, 156.3)
- added R7: 1k, Capacitor_SMD:C_0603_1608Metric, F.Cu at (134.0, 131.3)
- added R7: 1k, Capacitor_SMD:C_0603_1608Metric, F.Cu at (84.0, 131.3)
- added R7: 1k, Capacitor_SMD:C_0603_1608Metric, F.Cu at (134.0, 106.3)
- added R7: 1k, Capacitor_SMD:C_0603_1608Metric, F.Cu at (84.0, 106.3)
- added R7: 1k, Capacitor_SMD:C_0603_1608Metric, F.Cu at (134.0, 81.3)
- added R8: 4k, Capacitor_SMD:C_0603_1608Metric, F.Cu at (99.0, 159.6)
- added R8: 4k, Capacitor_SMD:C_0603_1608Metric, F.Cu at (49.0, 159.6)
- added R8: 4k, Capacitor_SMD:C_0603_1608Metric, F.Cu at (99.0, 134.6)
- added R8: 4k, Capacitor_SMD:C_0603_1608Metric, F.Cu at (49.0, 134.6)
- added R8: 4k, Capacitor_SMD:C_0603_1608Metric, F.Cu at (99.0, 109.6)
- added R8: 4k, Capacitor_SMD:C_0603_1608Metric, F.Cu at (49.0, 109.6)
- added R8: 4k, Capacitor_SMD:C_0603_1608Metric, F.Cu at (99.0, 84.6)
- added R9: 1k, Capacitor_SMD:C_0603_1608Metric, F.Cu at (132.7, 158.8)
- added R9: 1k, Capacitor_SMD:C_0603_1608Metric, F.Cu at (82.7, 158.8)
- added R9: 1k, Capacitor_SMD:C_0603_1608Metric, F.Cu at (132.7, 133.8)
- added R9: 1k, Capacitor_SMD:C_0603_1608Metric, F.Cu at (82.7, 133.8)
- added R9: 1k, Capacitor_SMD:C_0603_1608Metric, F.Cu at (132.7, 108.8)
- added R9: 1k, Capacitor_SMD:C_0603_1608Metric, F.Cu at (82.7, 108.8)
- added R9: 1k, Capacitor_SMD:C_0603_1608Metric, F.Cu at (132.7, 83.8)
- added U1: FD6288T, Package_SO:TSSOP-20_4.4x6.5mm_P0.65mm, F.Cu at (127.1, 148.9)
- added U1: FD6288T, Package_SO:TSSOP-20_4.4x6.5mm_P0.65mm, F.Cu at (77.1, 148.9)
- added U1: FD6288T, Package_SO:TSSOP-20_4.4x6.5mm_P0.65mm, F.Cu at (127.1, 123.9)
- added U1: FD6288T, Package_SO:TSSOP-20_4.4x6.5mm_P0.65mm, F.Cu at (77.1, 123.9)
- added U1: FD6288T, Package_SO:TSSOP-20_4.4x6.5mm_P0.65mm, F.Cu at (127.1, 98.9)
- added U1: FD6288T, Package_SO:TSSOP-20_4.4x6.5mm_P0.65mm, F.Cu at (77.1, 98.9)
- added U1: FD6288T, Package_SO:TSSOP-20_4.4x6.5mm_P0.65mm, F.Cu at (127.1, 73.9)
- added U2: LM1117-5.0, Package_TO_SOT_SMD:SOT-223, B.Cu at (135.6, 159.4)
- added U2: LM1117-5.0, Package_TO_SOT_SMD:SOT-223, B.Cu at (85.6, 159.4)
- added U2: LM1117-5.0, Package_TO_SOT_SMD:SOT-223, B.Cu at (135.6, 134.4)
- added U2: LM1117-5.0, Package_TO_SOT_SMD:SOT-223, B.Cu at (85.6, 134.4)
- added U2: LM1117-5.0, Package_TO_SOT_SMD:SOT-223, B.Cu at (135.6, 109.4)
- added U2: LM1117-5.0, Package_TO_SOT_SMD:SOT-223, B.Cu at (85.6, 109.4)
- added U2: LM1117-5.0, Package_TO_SOT_SMD:SOT-223, B.Cu at (135.6, 84.4)
- added U3: LM1117-3.3, Package_TO_SOT_SMD:SOT-223, B.Cu at (126.5, 159.6)
- added U3: LM1117-3.3, Package_TO_SOT_SMD:SOT-223, B.Cu at (76.5, 159.6)
- added U3: LM1117-3.3, Package_TO_SOT_SMD:SOT-223, B.Cu at (126.5, 134.6)
- added U3: LM1117-3.3, Package_TO_SOT_SMD:SOT-223, B.Cu at (76.5, 134.6)
- added U3: LM1117-3.3, Package_TO_SOT_SMD:SOT-223, B.Cu at (126.5, 109.6)
- added U3: LM1117-3.3, Package_TO_SOT_SMD:SOT-223, B.Cu at (76.5, 109.6)
- added U3: LM1117-3.3, Package_TO_SOT_SMD:SOT-223, B.Cu at (126.5, 84.6)
- moved U3 53.2 mm to (76.5, 84.6), turned to 270 degrees
- moved C8 52.8 mm to (81.0, 87.5), turned to 90 degrees
- moved C7 50.7 mm to (82.7, 87.5), turned to 270 degrees
- moved C10 48.0 mm to (73.5, 79.4), turned to 180 degrees
- moved R17 43.8 mm to (68.2, 82.4)
- moved R15 43.8 mm to (68.2, 84.2)
- moved Q5 42.7 mm to (66.3, 83.1), turned to 90 degrees
- moved R16 40.7 mm to (68.2, 80.5), turned to 180 degrees
- moved IC1 40.6 mm to (75.6, 83.2), turned to 90 degrees
- moved R5 39.1 mm to (63.2, 82.4), turned to 270 degrees
- moved R12 38.3 mm to (57.8, 84.5)
- moved R14 38.3 mm to (57.8, 82.5)
- moved R6 37.0 mm to (65.9, 77.6), turned to 180 degrees
- moved R8 36.8 mm to (49.0, 84.6)
- moved R11 36.6 mm to (49.0, 82.7)
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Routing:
- net GND: track 501.9 -> 1026.7 mm, vias 18 -> 64
- net MOTOR_A: track 195.8 -> 528.0 mm, vias 21 -> 32
- net +BATT: track 352.9 -> 643.0 mm, vias 18 -> 40
- net MOTOR_B: track 195.6 -> 471.9 mm, vias 18 -> 24
- net MOTOR_C: track 239.0 -> 487.7 mm, vias 15 -> 24
- net COM_ALL: track 76.5 -> 321.6 mm, vias 15 -> 48
- net LO1: track 121.7 -> 337.0 mm, vias 24 -> 0
- net LO2: track 88.3 -> 296.7 mm, vias 6 -> 16
- net MUX_A: track 94.4 -> 258.2 mm, vias 12 -> 0
- net MUX_B: track 69.8 -> 181.2 mm, vias 12 -> 0
- net VB1: track 56.0 -> 167.3 mm, vias 3 -> 8
- net LO3: track 81.1 -> 181.5 mm, vias 6 -> 16
- net HO1: track 162.1 -> 259.2 mm, vias 24 -> 0
- net +3V3: track 239.3 -> 165.0 mm, vias 15 -> 8
- net HIN3: track 23.7 -> 94.4 mm, vias 6 -> 16
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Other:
- board size 61 x 99.6 mm -> 99.5 x 99.1 mm
